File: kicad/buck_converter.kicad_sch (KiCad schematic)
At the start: 46 parts, among them J5 SolderPad, J6 SolderPad, Q2 CSD19537Q3, Q3 BSZ096N10LS5, U2 LM5146

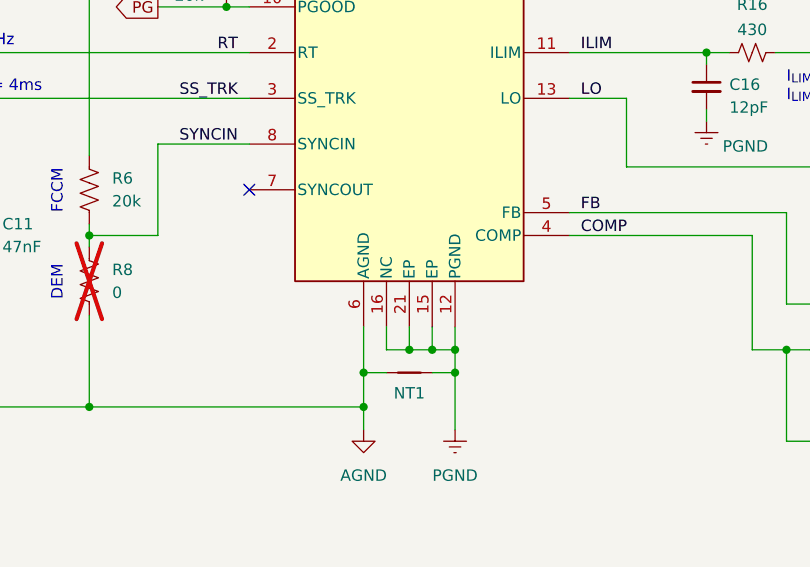
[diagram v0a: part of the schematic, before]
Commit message: Layout tweaks, added copyright notice
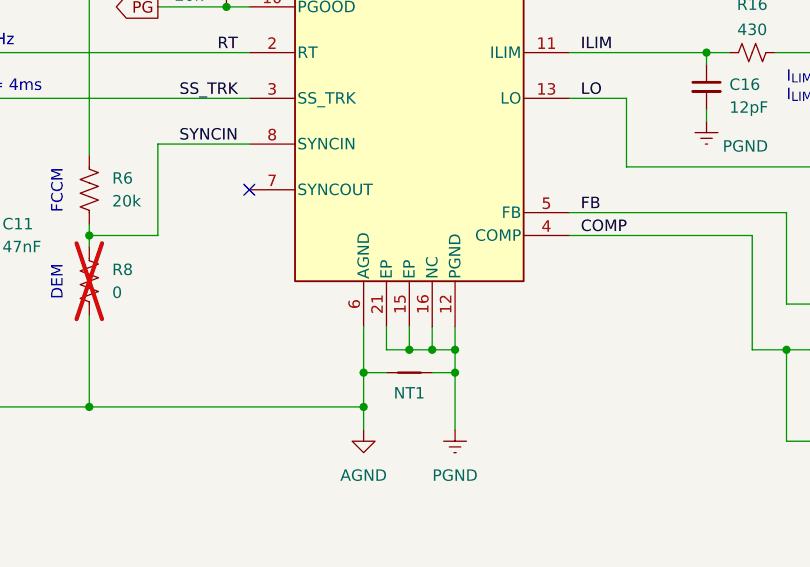
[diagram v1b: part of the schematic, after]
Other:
- company: Julian Joaquin -> Author: Julian Joaquin
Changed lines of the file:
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@@
 	(title_block
 		(title "Super Step Down V3")
-		(date "2025-11-04")
+		(date "2025-11-08")
 		(rev "D")
-		(company "Julian Joaquin")
-		(comment 1 "A 12S battery eliminator circuit (BEC) for UAS applications.")
+		(company "Author: Julian Joaquin")
+		(comment 1 "Licensed under CERN-OHL-W version 2")
+		(comment 2 "Copyright © Julian Joaquin, 2025")
+		(comment 4 "A 12S battery eliminator circuit (BEC) for UAS applications.")
 	)
 	(text "capacitor zeros:\nf_{ESR1} = 88.9kHz\nf_{ESR2} = 2.53MHz @ 5V\n\ncapacitor poles:\nf_{parallel} = 167kHz @ 5V"
@@
 	)
 	(symbol
-		(lib_name "LM5146RGYR_1")
 		(lib_id "Julian_Symbols:LM5146RGYR")
 		(at 87.63 83.82 0)
